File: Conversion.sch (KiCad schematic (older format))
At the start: 3 parts, among them U6 TXS0108EPWR

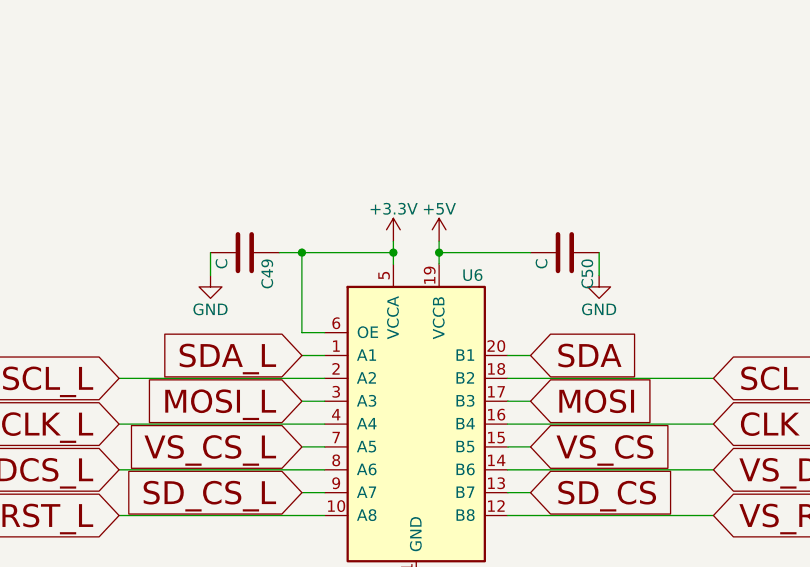
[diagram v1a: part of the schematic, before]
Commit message: Board modified after ckecking. Ready for fab, just need to create gerber, position and components files.
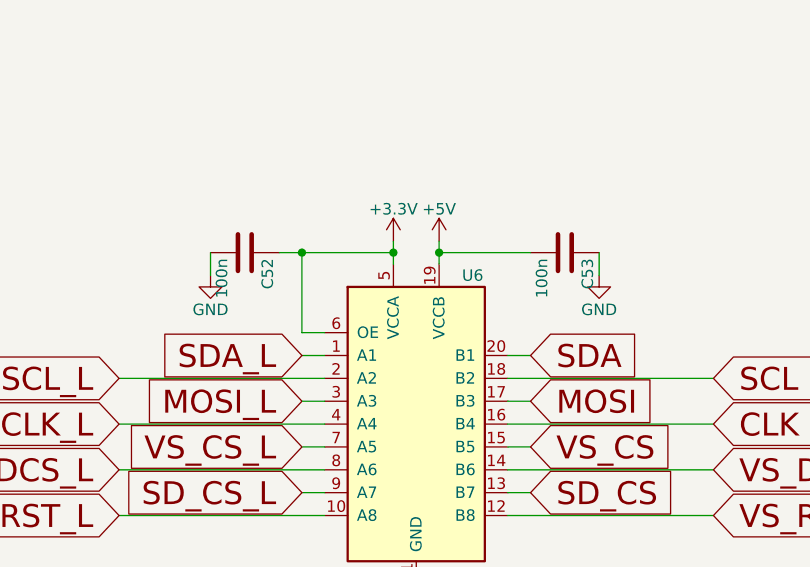
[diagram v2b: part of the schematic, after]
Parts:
- C52: renamed from C49; value C -> 100n
- C53: renamed from C50; value C -> 100n
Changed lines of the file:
@@
 EESchema Schematic File Version 2
+LIBS:ContactConsequencesMono-rescue
 LIBS:switches-perso
 LIBS:Logos
@@
 $EndComp
 $Comp
-L +5V #PWR075
+L +5V #PWR083
 U 1 1 59B191A1
 P 5600 2500
-F 0 "#PWR075" H 5600 2350 50  0001 C CNN
+F 0 "#PWR083" H 5600 2350 50  0001 C CNN
 F 1 "+5V" H 5600 2640 50  0000 C CNN
 F 2 "" H 5600 2500 50  0001 C CNN
@@
 $EndComp
 $Comp
-L +3.3V #PWR076
+L +3.3V #PWR084
 U 1 1 59B191F6
 P 5400 2500
-F 0 "#PWR076" H 5400 2350 50  0001 C CNN
+F 0 "#PWR084" H 5400 2350 50  0001 C CNN
 F 1 "+3.3V" H 5400 2640 50  0000 C CNN
 F 2 "" H 5400 2500 50  0001 C CNN
@@
 	5900 3700 6800 3700
 $Comp
-L GND #PWR077
+L GND #PWR085
 U 1 1 59B1A768
 P 5500 4100
-F 0 "#PWR077" H 5500 3850 50  0001 C CNN
+F 0 "#PWR085" H 5500 3850 50  0001 C CNN
 F 1 "GND" H 5500 3950 50  0000 C CNN
 F 2 "" H 5500 4100 50  0001 C CNN
@@
 Connection ~ 5400 2550
 $Comp
-L GND #PWR078
+L GND #PWR086
 U 1 1 59B1AFF7
 P 4600 2650
-F 0 "#PWR078" H 4600 2400 50  0001 C CNN
+F 0 "#PWR086" H 4600 2400 50  0001 C CNN
 F 1 "GND" H 4600 2500 50  0000 C CNN
 F 2 "" H 4600 2650 50  0001 C CNN
@@
 $EndComp
 $Comp
-L C C49
+L C C52
 U 1 1 59B1B00E
 P 4750 2550
-F 0 "C49" H 4775 2650 50  0000 L CNN
-F 1 "C" H 4775 2450 50  0000 L CNN
+F 0 "C52" H 4775 2650 50  0000 L CNN
+F 1 "100n" H 4775 2450 50  0000 L CNN
 F 2 "Capacitors_SMD:C_0603" H 4788 2400 50  0001 C CNN
 F 3 "" H 4750 2550 50  0001 C CNN
@@
 $EndComp
 $Comp
-L C C50
+L C C53
 U 1 1 59B1B05E
 P 6150 2550
-F 0 "C50" H 6175 2650 50  0000 L CNN
-F 1 "C" H 6175 2450 50  0000 L CNN
+F 0 "C53" H 6175 2650 50  0000 L CNN
+F 1 "100n" H 6175 2450 50  0000 L CNN
 F 2 "Capacitors_SMD:C_0603" H 6188 2400 50  0001 C CNN
 F 3 "" H 6150 2550 50  0001 C CNN
@@
 	4600 2550 4600 2650
 $Comp
-L GND #PWR079
+L GND #PWR087
 U 1 1 59B1B16A
 P 6300 2650
-F 0 "#PWR079" H 6300 2400 50  0001 C CNN
+F 0 "#PWR087" H 6300 2400 50  0001 C CNN
 F 1 "GND" H 6300 2500 50  0000 C CNN
 F 2 "" H 6300 2650 50  0001 C CNN

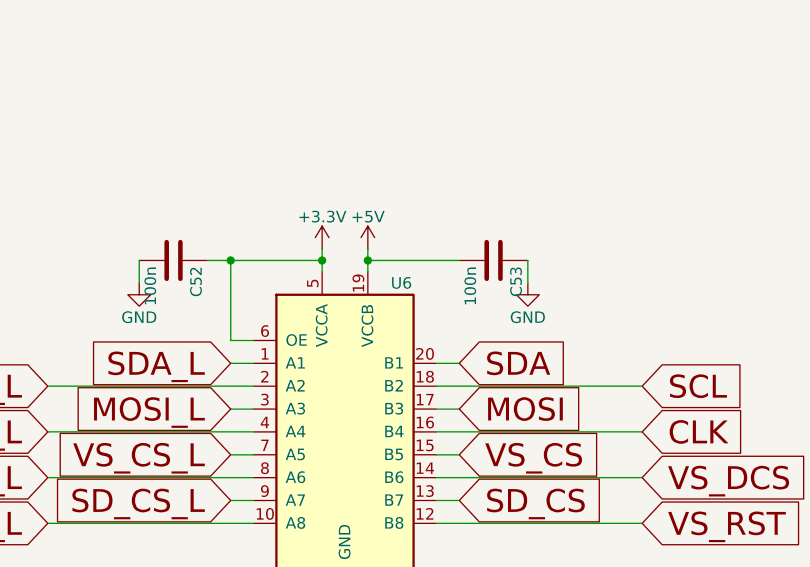
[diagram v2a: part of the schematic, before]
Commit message: v0.2 ready for fabrication. Voltage regulators replaced by cheaper ones.
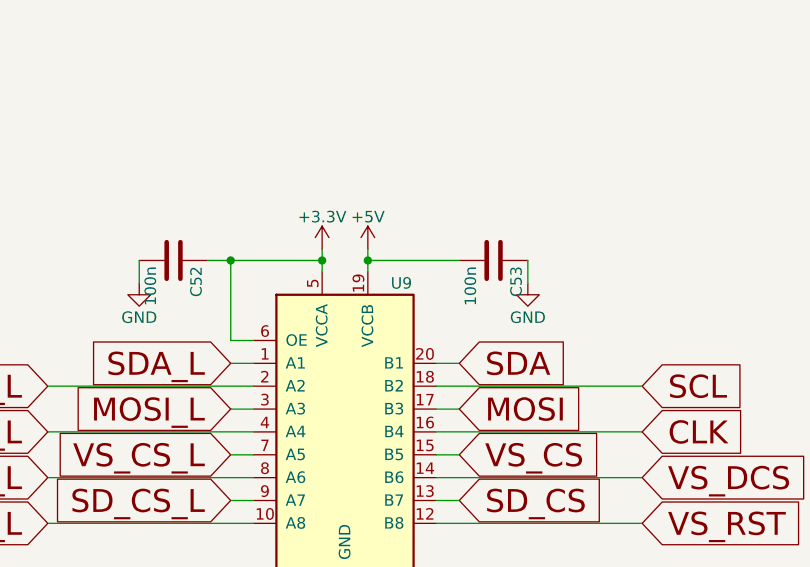
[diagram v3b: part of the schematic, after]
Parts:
- renumbered U6 to U9
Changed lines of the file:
@@
 VS_RST_L
 $Comp
-L TXS0108EPWR U6
+L TXS0108EPWR U9
 U 1 1 59B19046
 P 5500 3300
-F 0 "U6" H 5700 3950 50  0000 L CNN
+F 0 "U9" H 5700 3950 50  0000 L CNN
 F 1 "TXS0108EPWR" H 5600 2600 50  0000 L CNN
 F 2 "Housings_SSOP:TSSOP-20_4.4x6.5mm_Pitch0.65mm" H 5850 3750 50  0001 L CNN
